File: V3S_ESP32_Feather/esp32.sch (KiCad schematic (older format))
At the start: 23 parts, among them J2 PWM, J4 I2C, J5 U.FL-R-SMT(01), U3 MPU-9250_Obsolete, U5 ESP32-PICO-D4, U7 BMP280

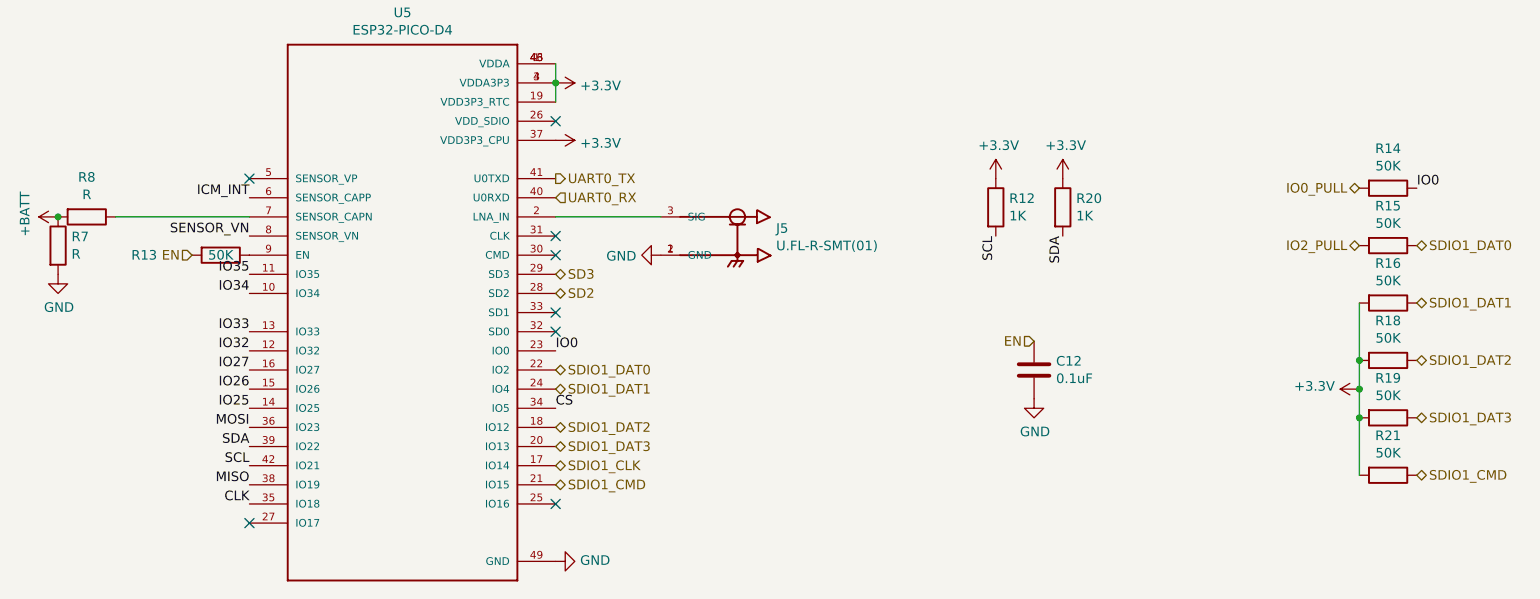
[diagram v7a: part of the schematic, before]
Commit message: routing done, started filling bom
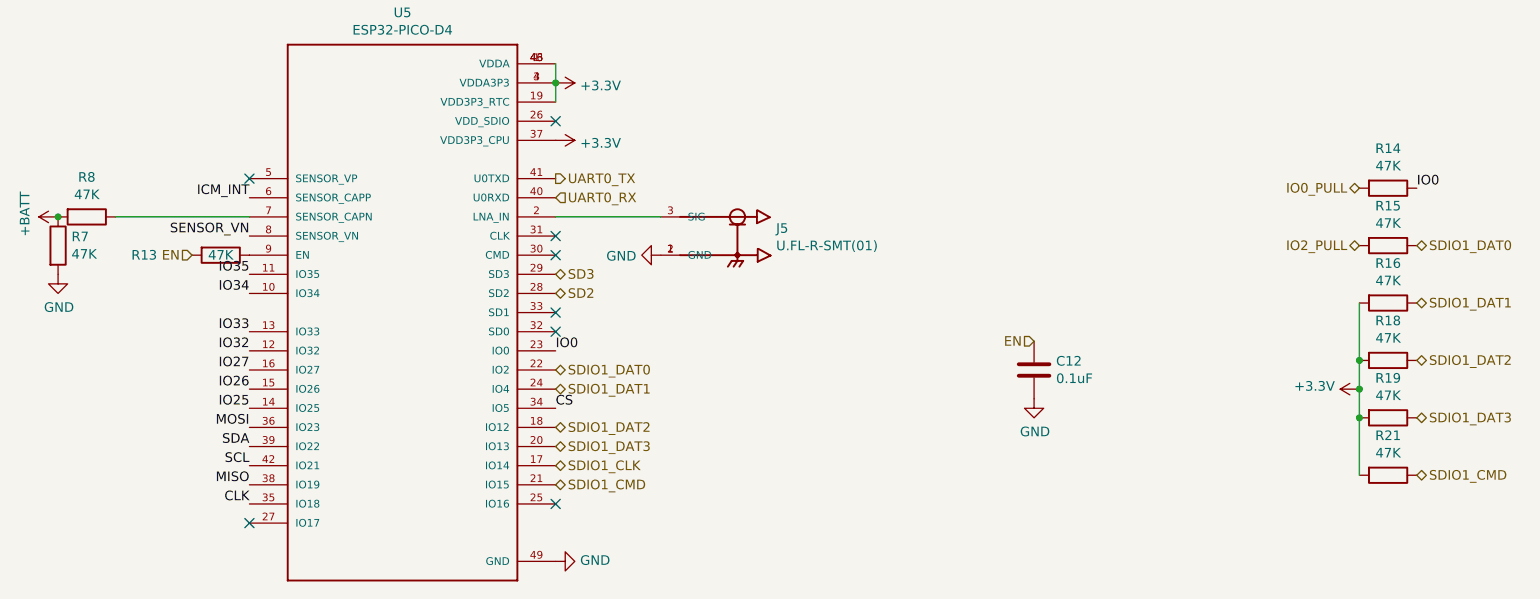
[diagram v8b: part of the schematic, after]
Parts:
- removed R12, R20: 1K, Resistor_SMD:R_0201_0603Metric, symbol Device:R
- R13, R14, R15, R16, R18, R19, R21: value 50K -> 47K
- R7, R8: value R -> 47K
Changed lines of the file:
@@
 P 1700 2700
 F 0 "R13" V 1700 2300 50  0000 C CNN
-F 1 "50K" V 1700 2700 50  0000 C CNN
+F 1 "47K" V 1700 2700 50  0000 C CNN
 F 2 "Resistor_SMD:R_0201_0603Metric" V 1630 2700 50  0001 C CNN
 F 3 "~" H 1700 2700 50  0001 C CNN
@@
 P 7800 2650
 F 0 "R15" V 7593 2650 50  0000 C CNN
-F 1 "50K" V 7684 2650 50  0000 C CNN
+F 1 "47K" V 7684 2650 50  0000 C CNN
 F 2 "Resistor_SMD:R_0201_0603Metric" V 7730 2650 50  0001 C CNN
 F 3 "~" H 7800 2650 50  0001 C CNN
@@
 P 7800 2950
 F 0 "R16" V 7593 2950 50  0000 C CNN
-F 1 "50K" V 7684 2950 50  0000 C CNN
+F 1 "47K" V 7684 2950 50  0000 C CNN
 F 2 "Resistor_SMD:R_0201_0603Metric" V 7730 2950 50  0001 C CNN
 F 3 "~" H 7800 2950 50  0001 C CNN
@@
 P 7800 3250
 F 0 "R18" V 7593 3250 50  0000 C CNN
-F 1 "50K" V 7684 3250 50  0000 C CNN
+F 1 "47K" V 7684 3250 50  0000 C CNN
 F 2 "Resistor_SMD:R_0201_0603Metric" V 7730 3250 50  0001 C CNN
 F 3 "~" H 7800 3250 50  0001 C CNN
@@
 P 7800 3550
 F 0 "R19" V 7593 3550 50  0000 C CNN
-F 1 "50K" V 7684 3550 50  0000 C CNN
+F 1 "47K" V 7684 3550 50  0000 C CNN
 F 2 "Resistor_SMD:R_0201_0603Metric" V 7730 3550 50  0001 C CNN
 F 3 "~" H 7800 3550 50  0001 C CNN
@@
 P 7800 3850
 F 0 "R21" V 7593 3850 50  0000 C CNN
-F 1 "50K" V 7684 3850 50  0000 C CNN
+F 1 "47K" V 7684 3850 50  0000 C CNN
 F 2 "Resistor_SMD:R_0201_0603Metric" V 7730 3850 50  0001 C CNN
 F 3 "~" H 7800 3850 50  0001 C CNN
@@
 P 7800 2350
 F 0 "R14" V 7593 2350 50  0000 C CNN
-F 1 "50K" V 7684 2350 50  0000 C CNN
+F 1 "47K" V 7684 2350 50  0000 C CNN
 F 2 "Resistor_SMD:R_0201_0603Metric" V 7730 2350 50  0001 C CNN
 F 3 "~" H 7800 2350 50  0001 C CNN
@@
 Text Label 2250 6150 2    50   ~ 0
 CLK
-$Comp
-L Device:R R?
-U 1 1 5D8381DE
-P 5750 2450
-AR Path="/5D8381DE" Ref="R?"  Part="1"
-AR Path="/5C7A02C5/5D8381DE" Ref="R12"  Part="1"
-F 0 "R12" H 5820 2496 50  0000 L CNN
-F 1 "1K" H 5820 2405 50  0000 L CNN
-F 2 "Resistor_SMD:R_0201_0603Metric" V 5680 2450 50  0001 C CNN
-F 3 "~" H 5750 2450 50  0001 C CNN
-	1    5750 2450
-	1    0    0    -1
-$EndComp
-$Comp
-L Device:R R?
-U 1 1 5D8381E4
-P 6100 2450
-AR Path="/5D8381E4" Ref="R?"  Part="1"
-AR Path="/5C7A02C5/5D8381E4" Ref="R20"  Part="1"
-F 0 "R20" H 6170 2496 50  0000 L CNN
-F 1 "1K" H 6170 2405 50  0000 L CNN
-F 2 "Resistor_SMD:R_0201_0603Metric" V 6030 2450 50  0001 C CNN
-F 3 "~" H 6100 2450 50  0001 C CNN
-	1    6100 2450
-	1    0    0    -1
-$EndComp
-$Comp
-L power:+3.3V #PWR?
-U 1 1 5D8381EA
-P 6100 2300
-AR Path="/5D8381EA" Ref="#PWR?"  Part="1"
-AR Path="/5C7A02C5/5D8381EA" Ref="#PWR0166"  Part="1"
-F 0 "#PWR0166" H 6100 2150 50  0001 C CNN
-F 1 "+3.3V" H 6115 2473 50  0000 C CNN
-F 2 "" H 6100 2300 50  0001 C CNN
-F 3 "" H 6100 2300 50  0001 C CNN
-	1    6100 2300
-	1    0    0    -1
-$EndComp
-$Comp
-L power:+3.3V #PWR?
-U 1 1 5D8381F0
-P 5750 2300
-AR Path="/5D8381F0" Ref="#PWR?"  Part="1"
-AR Path="/5C7A02C5/5D8381F0" Ref="#PWR0167"  Part="1"
-F 0 "#PWR0167" H 5750 2150 50  0001 C CNN
-F 1 "+3.3V" H 5765 2473 50  0000 C CNN
-F 2 "" H 5750 2300 50  0001 C CNN
-F 3 "" H 5750 2300 50  0001 C CNN
-	1    5750 2300
-	1    0    0    -1
-$EndComp
 NoConn ~ 1850 2300
 $Comp
@@
 P 850 2650
 F 0 "R7" H 920 2696 50  0000 L CNN
-F 1 "R" H 920 2605 50  0000 L CNN
+F 1 "47K" H 920 2605 50  0000 L CNN
 F 2 "Resistor_SMD:R_0201_0603Metric" V 780 2650 50  0001 C CNN
 F 3 "~" H 850 2650 50  0001 C CNN
@@
 P 1000 2500
 F 0 "R8" V 793 2500 50  0000 C CNN
-F 1 "R" V 884 2500 50  0000 C CNN
+F 1 "47K" V 884 2500 50  0000 C CNN
 F 2 "Resistor_SMD:R_0201_0603Metric" V 930 2500 50  0001 C CNN
 F 3 "~" H 1000 2500 50  0001 C CNN
@@
 Wire Wire Line
 	2350 5550 1950 5550
-Text Label 6100 2600 3    50   ~ 0
-SDA
-Text Label 5750 2600 3    50   ~ 0
-SCL
 Text Label 10400 3350 0    50   ~ 0
 SDA
